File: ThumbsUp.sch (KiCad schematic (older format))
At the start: 154 parts, among them IC1 RP2040, IC2 W25Q128JVSIM, IC3 RP2040, IC4 W25Q128JVSIM, J1 Conn_01x04_Male, J10 Raiser_Male, J11 Raiser_Female, J12 Raiser_Male, J13 Raiser_Female, J14 Raiser_Male, J15 Raiser_Female, J16 Raiser_Male, J17 Raiser_Female, J18 Raiser_Male, J19 Raiser_Female, J2 Conn_01x04_Male, J20 Conn_01x04_Female, J21 Conn_01x04_Female, J22 Conn_01x04_Female, J23 Conn_01x04_Female, J24 Conn_01x04_Male, J25 Conn_01x04_Male, J26 Conn_01x04_Male, J27 Conn_01x04_Male, J28 Conn_01x04_Female, J29 Conn_01x04_Female, J3 Conn_01x04_Female, J30 Conn_01x04_Female, J31 Conn_01x04_Female, J32 USB_C_Receptacle_USB2.0, J33 Raiser_Male, J34 Raiser_Female, J35 Raiser_Male, J36 STX-3501-3N, J37 USB_C_Receptacle_USB2.0, J38 Raiser_Female, J39 Raiser_Male, J4 Conn_01x04_Male, J40 Raiser_Female, J41 Raiser_Male, J42 Raiser_Female, J43 Raiser_Male, J44 Raiser_Female, J45 Raiser_Male, J46 STX-3501-3N, J47 Raiser_Female, J48 Raiser_Male, J5 Conn_01x04_Female, J6 Conn_01x04_Male, J7 Conn_01x04_Male, J8 Conn_01x04_Male, J9 Raiser_Female, U1 NCP1117-3.3_SOT223, U2 NCP1117-3.3_SOT223, Y1 ABLS-12.000MHZ-B4-T, Y2 ABLS-12.000MHZ-B4-T

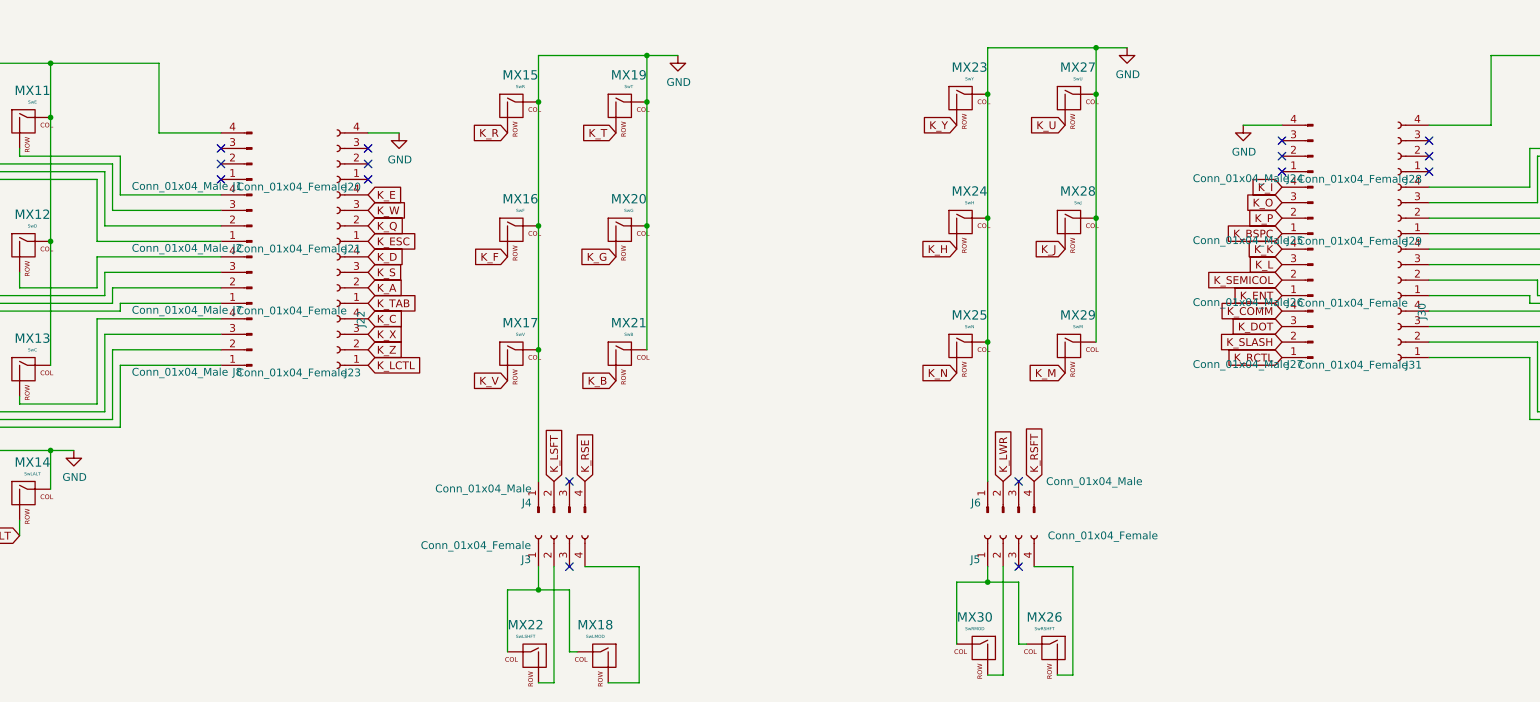
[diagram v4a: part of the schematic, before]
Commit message: Traced the top  and bottom plates.
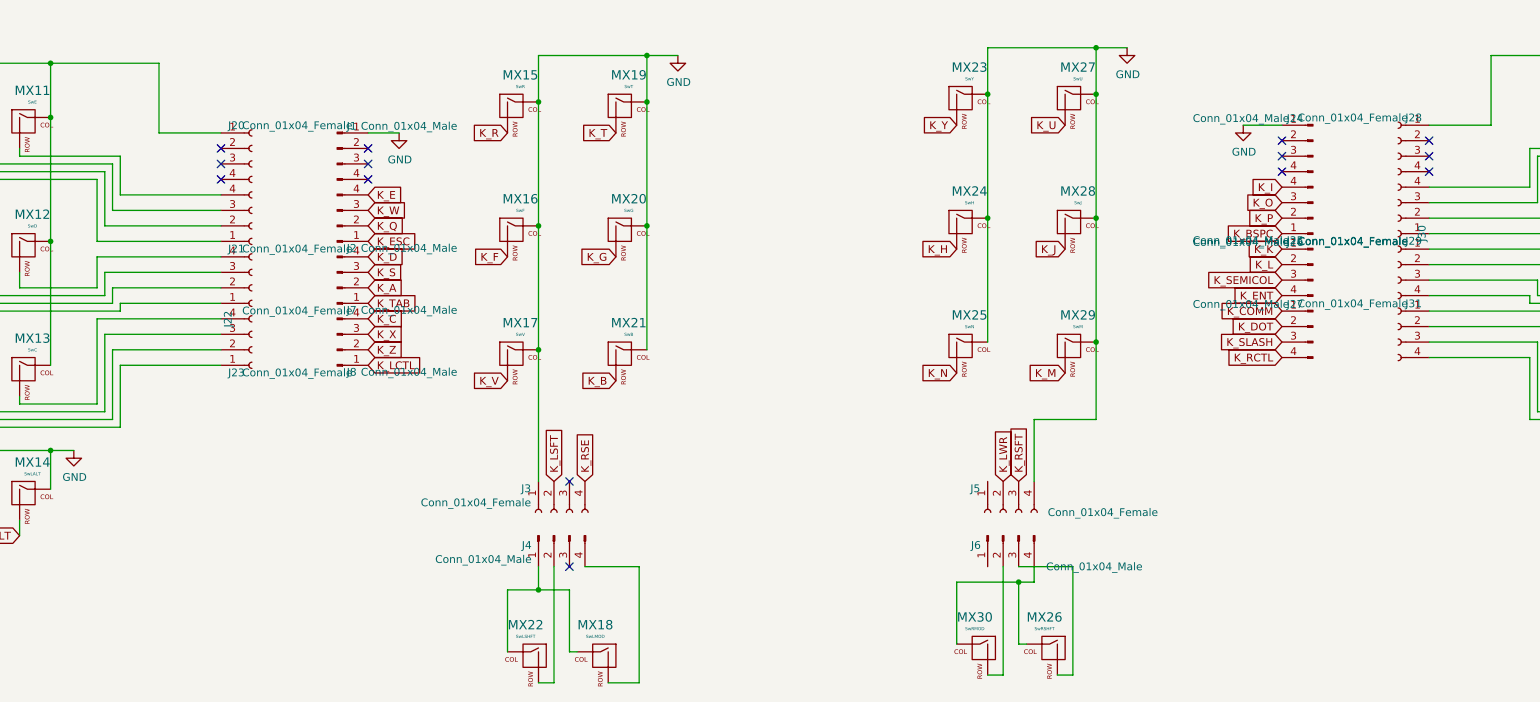
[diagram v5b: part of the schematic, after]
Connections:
- net GND: now also J1.1 (Pin_1), J24.1 (Pin_1), J3.1 (Pin_1), J5.4 (Pin_4); no longer J20.4 (Pin_4), J24.4 (Pin_4), J4.1 (Pin_1), J6.1 (Pin_1)
- net K_A: now also J7.2 (Pin_2); no longer J22.2 (Pin_2)
- net K_C: now also J8.4 (Pin_4); no longer J23.4 (Pin_4)
- net K_COMM: now also J27.1 (Pin_1); no longer J27.4 (Pin_4)
- net K_D: now also J7.4 (Pin_4); no longer J22.4 (Pin_4)
- net K_DOT: now also J27.2 (Pin_2); no longer J27.3 (Pin_3)
- net K_E: now also J2.4 (Pin_4); no longer J21.4 (Pin_4)
- net K_ENT: now also J26.4 (Pin_4); no longer J26.1 (Pin_1)
- net K_ESC: now also J2.1 (Pin_1); no longer J21.1 (Pin_1)
- net K_K: now also J26.1 (Pin_1); no longer J26.4 (Pin_4)
- net K_L: now also J26.2 (Pin_2); no longer J26.3 (Pin_3)
- net K_LCTL: now also J8.1 (Pin_1); no longer J23.1 (Pin_1)
- net K_LSFT: now also J3.2 (Pin_2); no longer J4.2 (Pin_2)
- net K_LWR: now also J5.2 (Pin_2); no longer J6.2 (Pin_2)
- net K_Q: now also J2.2 (Pin_2); no longer J21.2 (Pin_2)
- net K_RCTL: now also J27.4 (Pin_4); no longer J27.1 (Pin_1)
- net K_RSE: now also J3.4 (Pin_4); no longer J4.4 (Pin_4)
- net K_RSFT: now also J5.3 (Pin_3); no longer J6.4 (Pin_4)
- net K_S: now also J7.3 (Pin_3); no longer J22.3 (Pin_3)
- net K_SEMICOL: now also J26.3 (Pin_3); no longer J26.2 (Pin_2)
- net K_SLASH: now also J27.3 (Pin_3); no longer J27.2 (Pin_2)
- net K_TAB: now also J7.1 (Pin_1); no longer J22.1 (Pin_1)
- net K_W: now also J2.3 (Pin_3); no longer J21.3 (Pin_3)
- net K_X: now also J8.3 (Pin_3); no longer J23.3 (Pin_3)
- net K_Z: now also J8.2 (Pin_2); no longer J23.2 (Pin_2)
- net at MX1.1 (COL), MX11.1 (COL), MX12.1 (COL)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: now also J20.1 (Pin_1); no longer J1.4 (Pin_4)
- net at MX1.2 (ROW): now also J21.1 (Pin_1); no longer J2.1 (Pin_1)
- net at MX4.2 (ROW): now also J21.2 (Pin_2); no longer J2.2 (Pin_2)
- net at MX2.2 (ROW): now also J22.1 (Pin_1); no longer J7.1 (Pin_1)
- net at MX5.2 (ROW): now also J22.2 (Pin_2); no longer J7.2 (Pin_2)
- net at MX7.2 (ROW): now also J21.3 (Pin_3); no longer J2.3 (Pin_3)
- net at MX11.2 (ROW): now also J21.4 (Pin_4); no longer J2.4 (Pin_4)
- net at MX8.2 (ROW): now also J22.3 (Pin_3); no longer J7.3 (Pin_3)
- net at MX12.2 (ROW): now also J22.4 (Pin_4); no longer J7.4 (Pin_4)
- net at MX3.2 (ROW): now also J23.1 (Pin_1); no longer J8.1 (Pin_1)
- net at MX6.2 (ROW): now also J23.2 (Pin_2); no longer J8.2 (Pin_2)
- net at MX9.2 (ROW): now also J23.3 (Pin_3); no longer J8.3 (Pin_3)
- net at MX13.2 (ROW): now also J23.4 (Pin_4); no longer J8.4 (Pin_4)
- net at MX31.1 (COL), MX32.1 (COL), MX33.1 (COL)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: now also J28.1 (Pin_1); no longer J28.4 (Pin_4)
- net at MX43.2 (ROW): now also J30.4 (Pin_4); no longer J30.1 (Pin_1)
- net at MX36.2 (ROW): now also J30.2 (Pin_2); no longer J30.3 (Pin_3)
- net at MX32.2 (ROW): now also J30.1 (Pin_1); no longer J30.4 (Pin_4)
- net at MX44.2 (ROW): now also J31.4 (Pin_4); no longer J31.1 (Pin_1)
- net at MX41.2 (ROW): now also J31.3 (Pin_3); no longer J31.2 (Pin_2)
- net at MX37.2 (ROW): now also J31.2 (Pin_2); no longer J31.3 (Pin_3)
- net at MX33.2 (ROW): now also J31.1 (Pin_1); no longer J31.4 (Pin_4)
- net at MX40.2 (ROW): now also J30.3 (Pin_3); no longer J30.2 (Pin_2)
- net at MX18.1 (COL), MX22.1 (COL): now also J4.1 (Pin_1); no longer J3.1 (Pin_1)
- net at MX22.2 (ROW): now also J4.2 (Pin_2); no longer J3.2 (Pin_2)
- net at MX18.2 (ROW): now also J4.4 (Pin_4); no longer J3.4 (Pin_4)
- net at MX26.1 (COL), MX30.1 (COL): now also J6.4 (Pin_4); no longer J5.1 (Pin_1)
- net at MX30.2 (ROW): now also J6.2 (Pin_2); no longer J5.2 (Pin_2)
- net at MX26.2 (ROW): now also J6.3 (Pin_3); no longer J5.4 (Pin_4)
- no-connect marks 116 -> 114
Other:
- moved on the sheet: J1, J2, J20, J21, J22, J23, J3, J4, J5, J6, J7, J8

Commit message: Retracing the plates.
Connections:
- net GND: now also J2.4 (Pin_4); no longer J1.1 (Pin_1)
- net K_A: now also J16.2 (Pin_2); no longer J7.2 (Pin_2)
- net K_D: now also J16.4 (Pin_4); no longer J7.4 (Pin_4)
- net K_E: now also J45.4 (Pin_4); no longer J2.4 (Pin_4)
- net K_ESC: now also J45.1 (Pin_1); no longer J2.1 (Pin_1)
- net K_Q: now also J45.2 (Pin_2); no longer J2.2 (Pin_2)
- net K_S: now also J16.3 (Pin_3); no longer J7.3 (Pin_3)
- net K_TAB: now also J16.1 (Pin_1); no longer J7.1 (Pin_1)
- net K_W: now also J45.3 (Pin_3); no longer J2.3 (Pin_3)
- net at MX1.1 (COL), MX11.1 (COL), MX12.1 (COL)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: now also J21.4 (Pin_4); no longer J20.1 (Pin_1)
- net at MX1.2 (ROW): now also J44.1 (Pin_1); no longer J21.1 (Pin_1)
- net at MX4.2 (ROW): now also J44.2 (Pin_2); no longer J21.2 (Pin_2)
- net at MX2.2 (ROW): now also J15.1 (Pin_1); no longer J22.1 (Pin_1)
- net at MX5.2 (ROW): now also J15.2 (Pin_2); no longer J22.2 (Pin_2)
- net at MX7.2 (ROW): now also J44.3 (Pin_3); no longer J21.3 (Pin_3)
- net at MX11.2 (ROW): now also J44.4 (Pin_4); no longer J21.4 (Pin_4)
- net at MX8.2 (ROW): now also J15.3 (Pin_3); no longer J22.3 (Pin_3)
- net at MX12.2 (ROW): now also J15.4 (Pin_4); no longer J22.4 (Pin_4)
- no-connect marks 114 -> 98
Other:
- moved on the sheet: J1, J15, J16, J2, J20, J21, J22, J44, J45, J7
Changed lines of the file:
@@
 L Connector:Conn_01x04_Female J15
 U 1 1 6225ECEC
-P 21650 13600
-F 0 "J15" V 21496 13748 50  0000 L CNN
-F 1 "Raiser_Female" V 21587 13748 50  0000 L CNN
-F 2 "Connector_PinSocket_2.54mm:PinSocket_1x04_P2.54mm_Vertical" H 21650 13600 50  0001 C CNN
-F 3 "~" H 21650 13600 50  0001 C CNN
-	1    21650 13600
-	0    1    1    0
+P 5600 13100
+F 0 "J15" V 5700 13150 50  0000 L CNN
+F 1 "Raiser_Female" V 5537 13248 50  0000 L CNN
+F 2 "Connector_PinSocket_2.54mm:PinSocket_1x04_P2.54mm_Vertical" H 5600 13100 50  0001 C CNN
+F 3 "~" H 5600 13100 50  0001 C CNN
+	1    5600 13100
+	1    0    0    1
 $EndComp
 $Comp
 L Connector:Conn_01x04_Male J16
 U 1 1 6225ECF6
-P 21650 13750
-F 0 "J16" V 21712 13894 50  0000 L CNN
-F 1 "Raiser_Male" V 21803 13894 50  0000 L CNN
-F 2 "Connector_PinHeader_2.54mm:PinHeader_1x04_P2.54mm_Vertical" H 21650 13750 50  0001 C CNN
-F 3 "~" H 21650 13750 50  0001 C CNN
-	1    21650 13750
-	0    1    1    0
-$EndComp
-NoConn ~ 21450 13400
-NoConn ~ 21550 13400
-NoConn ~ 21650 13400
-NoConn ~ 21750 13400
-NoConn ~ 21450 13950
-NoConn ~ 21550 13950
-NoConn ~ 21650 13950
-NoConn ~ 21750 13950
+P 6150 13100
+F 0 "J16" V 6050 13150 50  0000 L CNN
+F 1 "Raiser_Male" V 6303 13244 50  0000 L CNN
+F 2 "Connector_PinHeader_2.54mm:PinHeader_1x04_P2.54mm_Vertical" H 6150 13100 50  0001 C CNN
+F 3 "~" H 6150 13100 50  0001 C CNN
+	1    6150 13100
+	1    0    0    1
+$EndComp
 Wire Wire Line
 	2200 11650 2200 12000
@@
 L Connector:Conn_01x04_Male J7
 U 1 1 6355EACB
-P 6150 13100
-F 0 "J7" H 6212 13244 50  0000 L CNN
-F 1 "Conn_01x04_Male" H 6303 13244 50  0000 L CNN
-F 2 "Connector_PinHeader_2.54mm:PinHeader_1x04_P2.54mm_Vertical" H 6150 13100 50  0001 C CNN
-F 3 "~" H 6150 13100 50  0001 C CNN
-	1    6150 13100
+P 6150 13950
+F 0 "J7" H 6212 14094 50  0000 L CNN
+F 1 "Conn_01x04_Male" H 6303 14094 50  0000 L CNN
+F 2 "Connector_PinHeader_2.54mm:PinHeader_1x04_P2.54mm_Vertical" H 6150 13950 50  0001 C CNN
+F 3 "~" H 6150 13950 50  0001 C CNN
+	1    6150 13950
 	1    0    0    1
 $EndComp
@@
 L Connector:Conn_01x04_Male J2
 U 1 1 63651670
-P 6150 12700
-F 0 "J2" H 6212 12844 50  0000 L CNN
-F 1 "Conn_01x04_Male" H 6303 12844 50  0000 L CNN
-F 2 "Connector_PinHeader_2.54mm:PinHeader_1x04_P2.54mm_Vertical" H 6150 12700 50  0001 C CNN
-F 3 "~" H 6150 12700 50  0001 C CNN
-	1    6150 12700
-	1    0    0    1
-$EndComp
-$Comp
-L Connector:Conn_01x04_Female J21
-U 1 1 63650D67
-P 5600 12700
-F 0 "J21" H 5446 12848 50  0000 L CNN
-F 1 "Conn_01x04_Female" H 5537 12848 50  0000 L CNN
-F 2 "Connector_PinSocket_2.54mm:PinSocket_1x04_P2.54mm_Vertical" H 5600 12700 50  0001 C CNN
-F 3 "~" H 5600 12700 50  0001 C CNN
-	1    5600 12700
+P 6150 12300
+F 0 "J2" H 5950 12250 50  0000 L CNN
+F 1 "Conn_01x04_Male" V 6100 12000 50  0000 L CNN
+F 2 "Connector_PinHeader_2.54mm:PinHeader_1x04_P2.54mm_Vertical" H 6150 12300 50  0001 C CNN
+F 3 "~" H 6150 12300 50  0001 C CNN
+	1    6150 12300
 	1    0    0    1
 $EndComp
@@
 L Connector:Conn_01x04_Female J22
 U 1 1 6355FF0A
-P 5600 13100
-F 0 "J22" V 5446 13248 50  0000 L CNN
-F 1 "Conn_01x04_Female" H 5537 13248 50  0000 L CNN
-F 2 "Connector_PinSocket_2.54mm:PinSocket_1x04_P2.54mm_Vertical" H 5600 13100 50  0001 C CNN
-F 3 "~" H 5600 13100 50  0001 C CNN
-	1    5600 13100
+P 5650 13950
+F 0 "J22" V 5496 14098 50  0000 L CNN
+F 1 "Conn_01x04_Female" H 5587 14098 50  0000 L CNN
+F 2 "Connector_PinSocket_2.54mm:PinSocket_1x04_P2.54mm_Vertical" H 5650 13950 50  0001 C CNN
+F 3 "~" H 5650 13950 50  0001 C CNN
+	1    5650 13950
 	1    0    0    1
 $EndComp
@@
 L Connector:Conn_01x04_Female J44
 U 1 1 63F46695
-P 21750 10900
-F 0 "J44" V 21596 11048 50  0000 L CNN
-F 1 "Raiser_Female" V 21687 11048 50  0000 L CNN
-F 2 "Connector_PinSocket_2.54mm:PinSocket_1x04_P2.54mm_Vertical" H 21750 10900 50  0001 C CNN
-F 3 "~" H 21750 10900 50  0001 C CNN
-	1    21750 10900
-	0    1    1    0
-$EndComp
-$Comp
-L Connector:Conn_01x04_Male J45
-U 1 1 63F4669B
-P 21750 11050
-F 0 "J45" V 21812 11194 50  0000 L CNN
-F 1 "Raiser_Male" V 21903 11194 50  0000 L CNN
-F 2 "Connector_PinHeader_2.54mm:PinHeader_1x04_P2.54mm_Vertical" H 21750 11050 50  0001 C CNN
-F 3 "~" H 21750 11050 50  0001 C CNN
-	1    21750 11050
-	0    1    1    0
-$EndComp
-NoConn ~ 21550 10700
-NoConn ~ 21650 10700
-NoConn ~ 21750 10700
-NoConn ~ 21850 10700
-NoConn ~ 21550 11250
-NoConn ~ 21650 11250
-NoConn ~ 21750 11250
-NoConn ~ 21850 11250
+P 5600 12700
+F 0 "J44" V 5700 12600 50  0000 L CNN
+F 1 "Raiser_Female" V 5537 12848 50  0000 L CNN
+F 2 "Connector_PinSocket_2.54mm:PinSocket_1x04_P2.54mm_Vertical" H 5600 12700 50  0001 C CNN
+F 3 "~" H 5600 12700 50  0001 C CNN
+	1    5600 12700
+	1    0    0    1
+$EndComp
 $Comp
 L STX-3501-3N:STX-3501-3N J46
@@
 $EndComp
 $Comp
+L Connector:Conn_01x04_Male J1
+U 1 1 6365127E
+P 6000 10700
+F 0 "J1" H 6062 10844 50  0000 L CNN
+F 1 "Conn_01x04_Male" H 6153 10844 50  0000 L CNN
+F 2 "Connector_PinHeader_2.54mm:PinHeader_1x04_P2.54mm_Vertical" H 6000 10700 50  0001 C CNN
+F 3 "~" H 6000 10700 50  0001 C CNN
+	1    6000 10700
+	1    0    0    -1
+$EndComp
+Wire Wire Line
+	10150 15000 10550 15000
+Wire Wire Line
+	10650 14900 10650 15000
+Wire Wire Line
+	10650 15000 10550 15000
+Connection ~ 10550 15000
+Wire Wire Line
+	10650 14350 10650 13950
+Wire Wire Line
+	10650 13950 11050 13950
+Wire Wire Line
+	11050 13950 11050 13450
+Connection ~ 11050 13450
+Wire Wire Line
+	10900 14900 10900 15600
+Wire Wire Line
+	10550 14900 10900 14900
+Wire Wire Line
+	7750 14900 8100 14900
+$Comp
+L Connector:Conn_01x04_Male J45
+U 1 1 63F4669B
+P 6150 12700
+F 0 "J45" V 6050 12600 50  0000 L CNN
+F 1 "Raiser_Male" V 6303 12844 50  0000 L CNN
+F 2 "Connector_PinHeader_2.54mm:PinHeader_1x04_P2.54mm_Vertical" H 6150 12700 50  0001 C CNN
+F 3 "~" H 6150 12700 50  0001 C CNN
+	1    6150 12700
+	1    0    0    1
+$EndComp
+$Comp
+L Connector:Conn_01x04_Female J21
+U 1 1 63650D67
+P 5600 12300
+F 0 "J21" H 5700 12250 50  0000 L CNN
+F 1 "Conn_01x04_Female" V 5650 11850 50  0000 L CNN
+F 2 "Connector_PinSocket_2.54mm:PinSocket_1x04_P2.54mm_Vertical" H 5600 12300 50  0001 C CNN
+F 3 "~" H 5600 12300 50  0001 C CNN
+	1    5600 12300
+	1    0    0    1
+$EndComp
+$Comp
 L Connector:Conn_01x04_Female J20
 U 1 1 6364D01C
-P 5600 12200
-F 0 "J20" H 5446 12348 50  0000 L CNN
-F 1 "Conn_01x04_Female" H 5537 12348 50  0000 L CNN
-F 2 "Connector_PinSocket_2.54mm:PinSocket_1x04_P2.54mm_Vertical" H 5600 12200 50  0001 C CNN
-F 3 "~" H 5600 12200 50  0001 C CNN
-	1    5600 12200
-	1    0    0    -1
-$EndComp
-$Comp
-L Connector:Conn_01x04_Male J1
-U 1 1 6365127E
-P 6150 12200
-F 0 "J1" H 6212 12344 50  0000 L CNN
-F 1 "Conn_01x04_Male" H 6303 12344 50  0000 L CNN
-F 2 "Connector_PinHeader_2.54mm:PinHeader_1x04_P2.54mm_Vertical" H 6150 12200 50  0001 C CNN
-F 3 "~" H 6150 12200 50  0001 C CNN
-	1    6150 12200
-	1    0    0    -1
-$EndComp
-Wire Wire Line
-	10150 15000 10550 15000
-Wire Wire Line
-	10650 14900 10650 15000
-Wire Wire Line
-	10650 15000 10550 15000
-Connection ~ 10550 15000
-Wire Wire Line
-	10650 14350 10650 13950
-Wire Wire Line
-	10650 13950 11050 13950
-Wire Wire Line
-	11050 13950 11050 13450
-Connection ~ 11050 13450
-Wire Wire Line
-	10900 14900 10900 15600
-Wire Wire Line
-	10550 14900 10900 14900
-Wire Wire Line
-	7750 14900 8100 14900
+P 5700 10750
+F 0 "J20" H 5546 10898 50  0000 L CNN
+F 1 "Conn_01x04_Female" V 5850 10350 50  0000 L CNN
+F 2 "Connector_PinSocket_2.54mm:PinSocket_1x04_P2.54mm_Vertical" H 5700 10750 50  0001 C CNN
+F 3 "~" H 5700 10750 50  0001 C CNN
+	1    5700 10750
+	1    0    0    -1
+$EndComp
 $EndSCHEMATC

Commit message: Tracing the plates.
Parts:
- C1, C10, C11, C12, C13, C14, C15, C16, C17, C18, C19, C2, C20, C21, C22, C23, C24, C25, C26, C27, C28, C29, C3, C30, C31, C32, C4, C5, C6, C7, C8, C9: footprint Capacitor_SMD:C_0805_2012Metric -> Capacitor_SMD:C_0402_1005Metric
- J36, J46: footprint STX35013N -> STX-3501-3N:STX35013N
- R1, R10, R11, R12, R13, R14, R15, R16, R2, R3, R6, R7, R8, R9: footprint Resistor_SMD:R_0805_2012Metric -> Resistor_SMD:R_0402_1005Metric
- R4, R5: value R -> 5.1K; footprint (none) -> Resistor_SMD:R_0402_1005Metric
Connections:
- net +3V3: no longer J36.3, J46.3
- net +5V: now also J36.3, J46.3
- net GND: now also J19.4 (Pin_4), J25.4 (Pin_4), J9.4 (Pin_4); no longer J24.1 (Pin_1)
- net K_BSPC: now also J43.1 (Pin_1); no longer J25.1 (Pin_1)
- net K_ENT: now also J12.4 (Pin_4); no longer J26.4 (Pin_4)
- net K_I: now also J43.4 (Pin_4); no longer J25.4 (Pin_4)
- net K_K: now also J12.1 (Pin_1); no longer J26.1 (Pin_1)
- net K_L: now also J12.2 (Pin_2); no longer J26.2 (Pin_2)
- net K_O: now also J43.3 (Pin_3); no longer J25.3 (Pin_3)
- net K_P: now also J43.2 (Pin_2); no longer J25.2 (Pin_2)
- net K_SEMICOL: now also J12.3 (Pin_3); no longer J26.3 (Pin_3)
- net +5VA: now reaches F1.2, J32.A4 (VBUS), J32.A9 (VBUS), J32.B4 (VBUS), J32.B9 (VBUS)
- net +5VA: now also F2.2, J37.A4 (VBUS), J37.A9 (VBUS), J37.B4 (VBUS), J37.B9 (VBUS)
- net at J11.1 (Pin_1): now also MX32.2 (ROW)
- net at J11.2 (Pin_2): now also MX36.2 (ROW)
- net at J11.3 (Pin_3): now also MX40.2 (ROW)
- net at J11.4 (Pin_4): now also MX43.2 (ROW)
- net at MX31.1 (COL), MX32.1 (COL), MX33.1 (COL)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: now also J29.4 (Pin_4); no longer J28.1 (Pin_1)
- net at MX42.2 (ROW): now also J42.1 (Pin_1); no longer J29.1 (Pin_1)
- net at MX39.2 (ROW): now also J42.2 (Pin_2); no longer J29.2 (Pin_2)
- net at J30.4 (Pin_4): no longer MX43.2 (ROW)
- net at MX35.2 (ROW): now also J42.3 (Pin_3); no longer J29.3 (Pin_3)
- net at MX31.2 (ROW): now also J42.4 (Pin_4); no longer J29.4 (Pin_4)
- net at J30.2 (Pin_2): no longer MX36.2 (ROW)
- net at J30.1 (Pin_1): no longer MX32.2 (ROW)
- net at J30.3 (Pin_3): no longer MX40.2 (ROW)
- net COL0: no longer names the net of IC1.35 (GPIO23)
- net COL0: no longer IC3.35 (GPIO23)
- net COL1: no longer names the net of IC1.36 (GPIO24)
- net COL1: no longer IC3.36 (GPIO24)
- net COL2: no longer names the net of IC1.37 (GPIO25)
- net COL2: no longer IC3.37 (GPIO25)
- net COL3: no longer names the net of IC1.38 (GPIO26/ADC0)
- net COL3: no longer IC3.38 (GPIO26/ADC0)
- net COL4: no longer names the net of IC1.34 (GPIO22)
- net COL4: no longer IC3.34 (GPIO22)
- net COL5: no longer names the net of IC1.39 (GPIO27/ADC1)
- net COL5: no longer IC3.39 (GPIO27/ADC1)
- net COL6: no longer names the net of IC1.5 (GPIO3)
- net COL6: no longer IC3.5 (GPIO3)
- net COL7: no longer names the net of IC1.4 (GPIO2)
- net COL7: no longer IC3.4 (GPIO2)
- net COL8: no longer names the net of IC1.6 (GPIO4)
- net COL8: no longer IC3.6 (GPIO4)
- net COL9: no longer names the net of IC1.7 (GPIO5)
- net COL9: no longer IC3.7 (GPIO5)
- net COLA: no longer names the net of IC1.8 (GPIO6)
- net COLA: no longer IC3.8 (GPIO6)
- net COLB: no longer names the net of IC1.9 (GPIO7)
- net COLB: no longer IC3.9 (GPIO7)
- net ROW1: no longer names the net of IC1.3 (GPIO1)
- net ROW1: no longer IC3.3 (GPIO1)
- net ROW2: no longer names the net of IC1.41 (GPIO29/ADC3)
- net ROW2: no longer IC3.41 (GPIO29/ADC3)
- net ROW3: no longer names the net of IC1.40 (GPIO28/ADC2)
- net ROW3: no longer IC3.40 (GPIO28/ADC2)
- no-connect marks 98 -> 96
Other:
- moved on the sheet: J11, J12, J24, J25, J26, J28, J29, J30, J42, J43

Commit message: Tracing the plates.
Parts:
- removed C30: 0.1uF, Capacitor_SMD:C_0402_1005Metric, symbol Device:C_Small
- R4, R5: value 5.1K -> DNF; footprint Resistor_SMD:R_0402_1005Metric -> Resistor_SMD:R_0805_2012Metric
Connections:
- net K_ENT: now also IC3.38 (GPIO26/ADC0)
- net K_K: now also IC3.41 (GPIO29/ADC3)
- net K_L: now also IC3.40 (GPIO28/ADC2)
- net K_LWR: now also IC3.36 (GPIO24)
- net K_RSFT: now also IC3.37 (GPIO25)
- net K_SEMICOL: now also IC3.39 (GPIO27/ADC1)
- net L-TIP: now also R4.1
- net R-TIP: now also R5.1
- net RTX: no longer names the net of IC3.2 (GPIO0)
- net RTX: no longer R5.1
- net TX: no longer names the net of IC1.2 (GPIO0)
- net TX: no longer R4.1
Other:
- moved on the sheet: J36, J46
